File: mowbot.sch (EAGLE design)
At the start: 20 parts, among them Q1 PSMN9R1-30YL-MOSFET_N, Q2 PSMN9R1-30YL-MOSFET_N, Q3 PSMN9R1-30YL-MOSFET_N, Q4 PSMN9R1-30YL-MOSFET_N, Q5 PSMN9R1-30YL-MOSFET_N, Q6 PSMN9R1-30YL-MOSFET_N, Q7 PSMN9R1-30YL-MOSFET_N, Q8 PSMN9R1-30YL-MOSFET_N

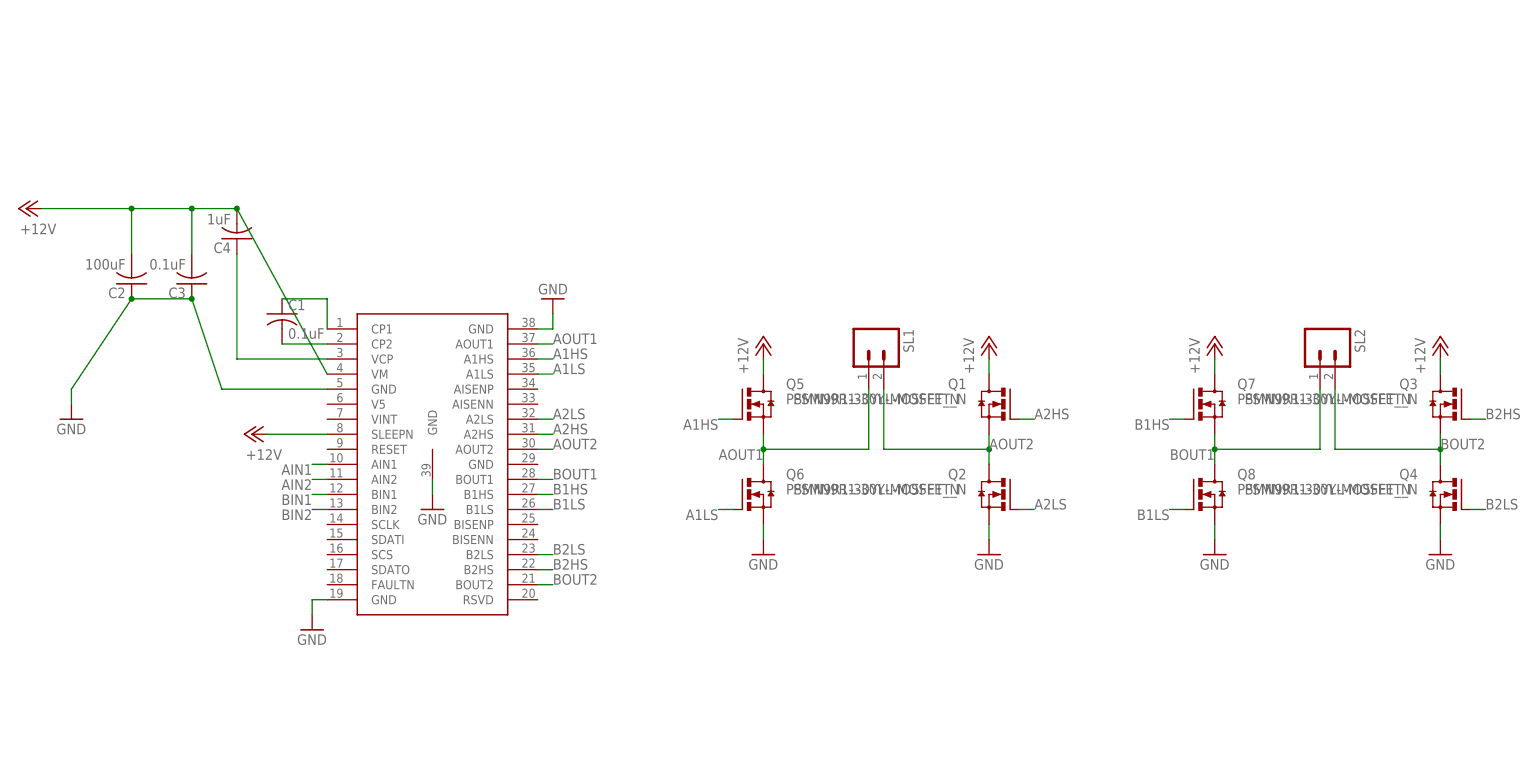
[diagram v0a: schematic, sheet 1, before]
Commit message: Arranged power FETs
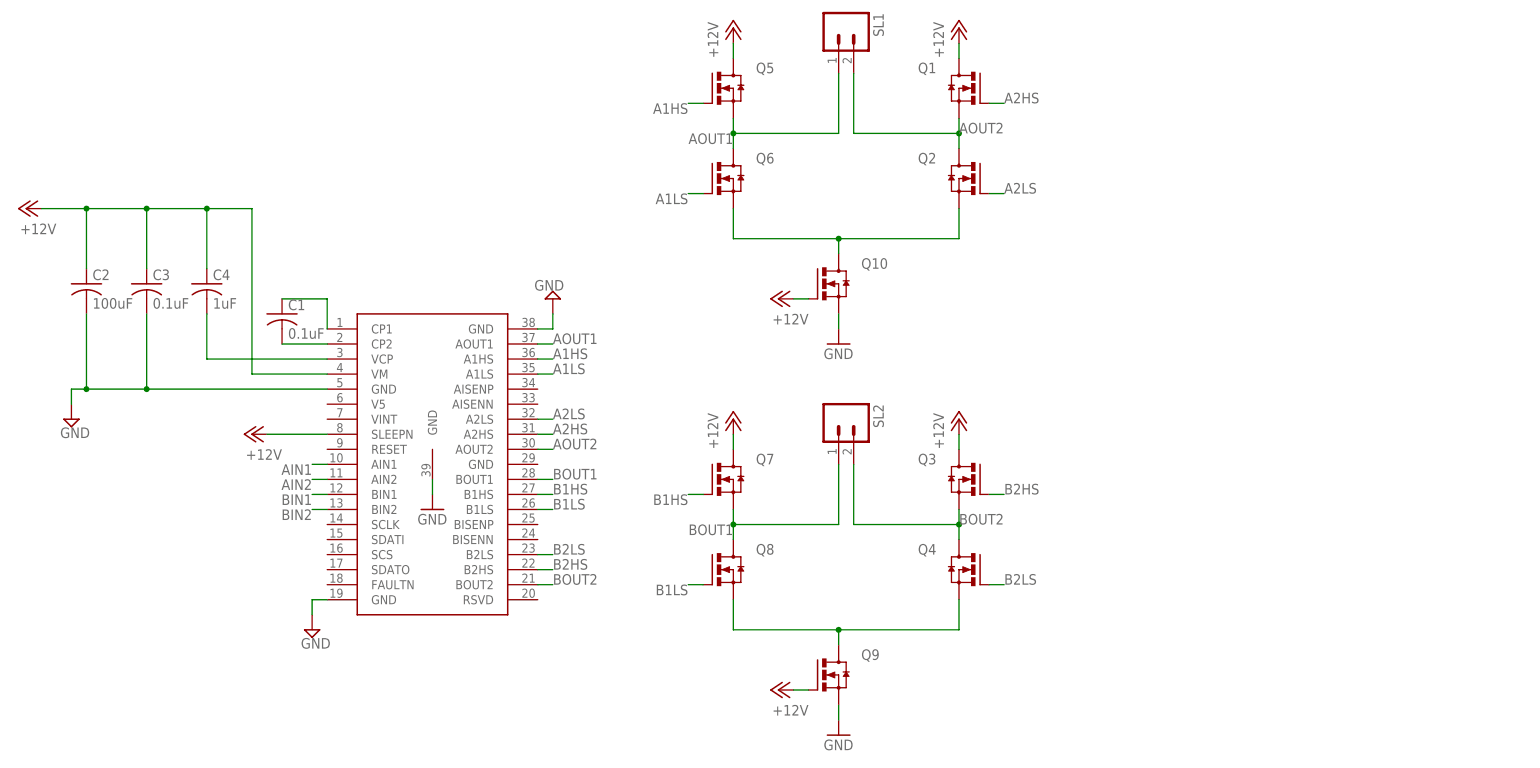
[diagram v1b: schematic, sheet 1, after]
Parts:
- added Q10, Q9: PSMN9R1-30YL-MOSFET_N, PSMN9R1-30YL_MOSFET_N:PSMN9R1-30YL-MOSFET_N
- added Q11: N-HEXFET_SOT323-, transistor-power:N-HEXFET_SOT323-
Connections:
- removed net N$7: C4.1, U$1.VCP
- new net N$2: C4.2, U$1.VCP
- new net N$4: Q4.S, Q8.S, Q9.D
- new net N$9: Q10.D, Q2.S, Q6.S
- net +12V: now also C2.1, C3.1, C4.1, Q10.G, Q11.G, Q9.G; no longer C2.2, C3.2, C4.2
- net GND: now also C2.2, C3.2, Q10.S, Q11.D, Q11.S, Q9.S; no longer C2.1, C3.1, Q2.S, Q4.S, Q6.S, Q8.S
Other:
- moved on the sheet: C2, C3, C4, Q1, Q2, Q3, Q4, Q5, Q6, Q7, Q8, SL1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

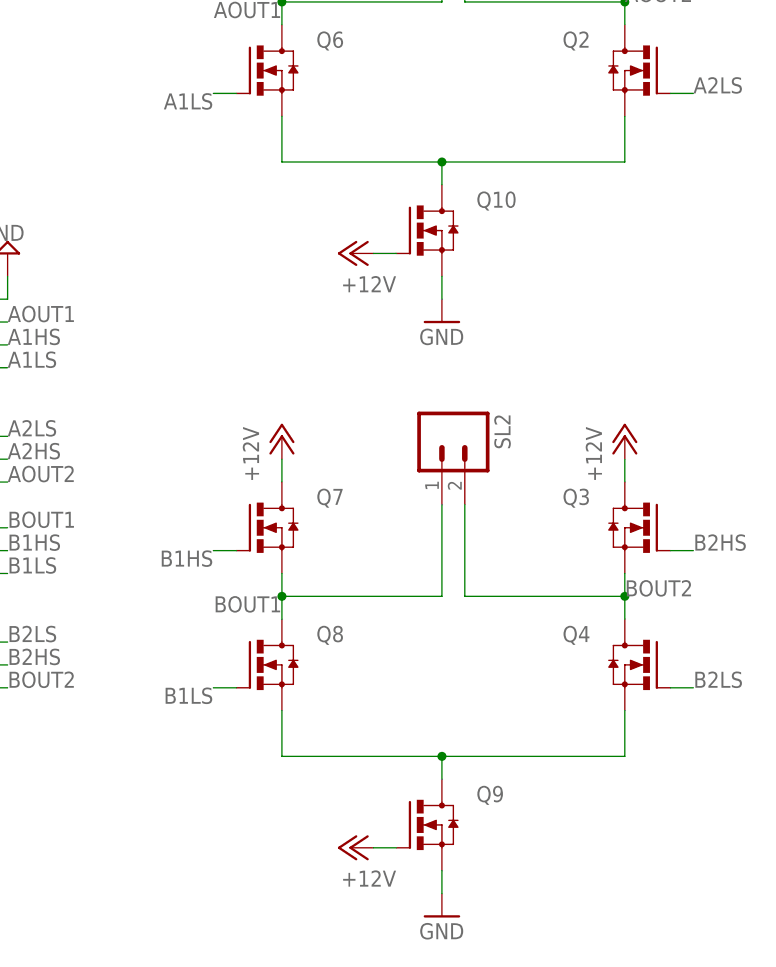
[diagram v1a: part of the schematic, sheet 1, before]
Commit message: Added reverse battery protection
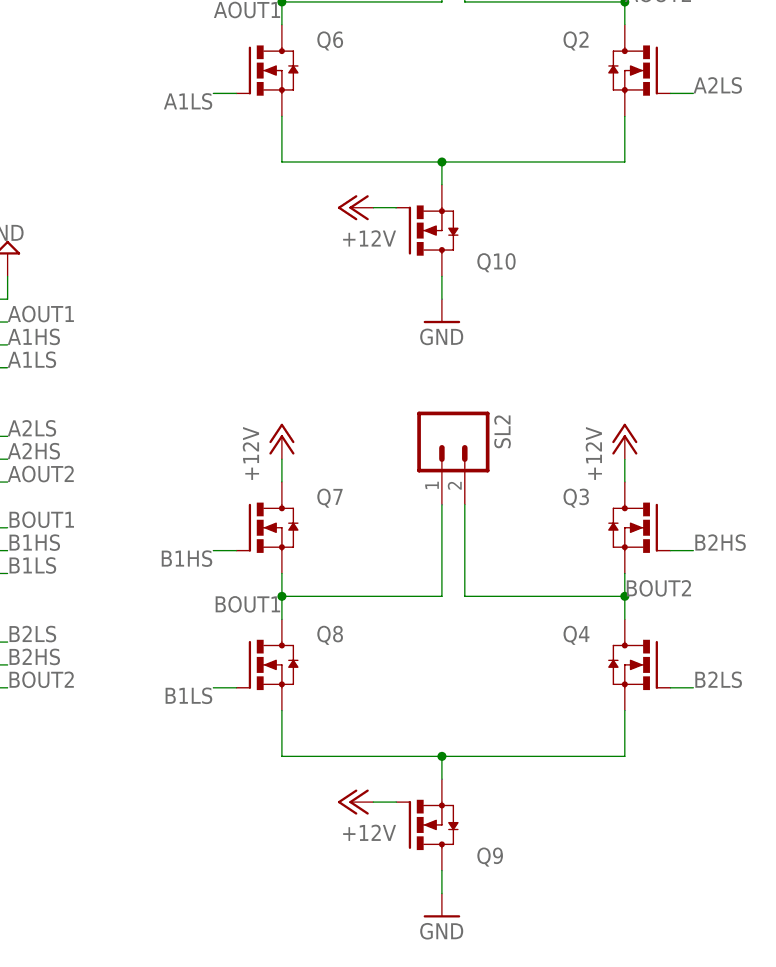
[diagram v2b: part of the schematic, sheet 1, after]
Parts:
- Q11: value N-HEXFET_SOT323- -> DMG2302UK-NMOSFET; device transistor-power:N-HEXFET_SOT323- -> DMG2302UK_NMOSFET:DMG2302UK-NMOSFET
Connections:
- net GND: now also Q10.D, Q9.D; no longer Q10.S, Q9.S
- net N$4: now also Q9.S; no longer Q9.D
- net N$9: now also Q10.S; no longer Q10.D
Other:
- moved on the sheet: Q10, Q9
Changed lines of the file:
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@@
 <part name="SUPPLY6" library="supply2" deviceset="GND" device=""/>
 <part name="SUPPLY7" library="supply2" deviceset="GND" device=""/>
-<part name="Q11" library="transistor-power" deviceset="N-HEXFET_?-*" device="SOT323"/>
+<part name="Q11" library="DMG2302UK_NMOSFET" deviceset="DMG2302UK-NMOSFET" device=""/>
 <part name="GND4" library="supply1" deviceset="GND" device=""/>
 <part name="P+10" library="supply1" deviceset="+12V" device=""/>
@@
 <instance part="C4" gate="G$1" x="-10.16" y="71.12"/>
 <instance part="P+6" gate="1" x="-2.54" y="45.72" rot="R90"/>
-<instance part="Q9" gate="G$1" x="93.98" y="5.08" smashed="yes">
-<attribute name="NAME" x="100.33" y="7.62" size="1.778" layer="95"/>
-</instance>
-<instance part="Q10" gate="G$1" x="93.98" y="71.12" smashed="yes">
-<attribute name="NAME" x="100.33" y="73.66" size="1.778" layer="95"/>
+<instance part="Q9" gate="G$1" x="93.98" y="5.08" smashed="yes" rot="MR180">
+<attribute name="NAME" x="100.33" y="2.54" size="1.778" layer="95" rot="MR180"/>
+</instance>
+<instance part="Q10" gate="G$1" x="93.98" y="71.12" smashed="yes" rot="MR180">
+<attribute name="NAME" x="100.33" y="68.58" size="1.778" layer="95" rot="MR180"/>
 </instance>
 <instance part="GND2" gate="1" x="96.52" y="-5.08"/>
-<instance part="P+8" gate="1" x="86.36" y="2.54" rot="R90"/>
+<instance part="P+8" gate="1" x="86.36" y="7.62" rot="R90"/>
 <instance part="GND3" gate="1" x="96.52" y="60.96"/>
-<instance part="P+9" gate="1" x="86.36" y="68.58" rot="R90"/>
+<instance part="P+9" gate="1" x="86.36" y="73.66" rot="R90"/>
 <instance part="SUPPLY5" gate="GND" x="-33.02" y="48.26"/>
 <instance part="SUPPLY6" gate="GND" x="7.62" y="12.7"/>
@@
 </segment>
 <segment>
+<pinref part="Q9" gate="G$1" pin="G"/>
 <pinref part="P+8" gate="1" pin="+12V"/>
-<pinref part="Q9" gate="G$1" pin="G"/>
-<wire x1="88.9" y1="2.54" x2="91.44" y2="2.54" width="0.1524" layer="91"/>
-</segment>
-<segment>
+<wire x1="91.44" y1="7.62" x2="88.9" y2="7.62" width="0.1524" layer="91"/>
+</segment>
+<segment>
+<pinref part="P+9" gate="1" pin="+12V"/>
 <pinref part="Q10" gate="G$1" pin="G"/>
-<pinref part="P+9" gate="1" pin="+12V"/>
-<wire x1="91.44" y1="68.58" x2="88.9" y2="68.58" width="0.1524" layer="91"/>
+<wire x1="88.9" y1="73.66" x2="91.44" y2="73.66" width="0.1524" layer="91"/>
 </segment>
 </net>
@@
 <pinref part="U$1" gate="G$1" pin="GND@5"/>
 <wire x1="27.94" y1="35.56" x2="27.94" y2="38.1" width="0.1524" layer="91"/>
-</segment>
-<segment>
-<pinref part="Q9" gate="G$1" pin="S"/>
-<pinref part="GND2" gate="1" pin="GND"/>
-<wire x1="96.52" y1="0" x2="96.52" y2="-2.54" width="0.1524" layer="91"/>
-</segment>
-<segment>
-<pinref part="Q10" gate="G$1" pin="S"/>
-<pinref part="GND3" gate="1" pin="GND"/>
-<wire x1="96.52" y1="66.04" x2="96.52" y2="63.5" width="0.1524" layer="91"/>
 </segment>
 <segment>
@@
 <pinref part="SUPPLY7" gate="GND" pin="GND"/>
 </segment>
+<segment>
+<pinref part="GND2" gate="1" pin="GND"/>
+<pinref part="Q9" gate="G$1" pin="D"/>
+<wire x1="96.52" y1="-2.54" x2="96.52" y2="0" width="0.1524" layer="91"/>
+</segment>
+<segment>
+<pinref part="Q10" gate="G$1" pin="D"/>
+<pinref part="GND3" gate="1" pin="GND"/>
+<wire x1="96.52" y1="66.04" x2="96.52" y2="63.5" width="0.1524" layer="91"/>
+</segment>
 </net>
 <net name="A1LS" class="0">
@@
 <pinref part="Q8" gate="G$1" pin="S"/>
 <wire x1="78.74" y1="12.7" x2="78.74" y2="17.78" width="0.1524" layer="91"/>
-<pinref part="Q9" gate="G$1" pin="D"/>
-<wire x1="96.52" y1="10.16" x2="96.52" y2="12.7" width="0.1524" layer="91"/>
-<wire x1="96.52" y1="12.7" x2="78.74" y2="12.7" width="0.1524" layer="91"/>
 <pinref part="Q4" gate="G$1" pin="S"/>
 <wire x1="116.84" y1="12.7" x2="116.84" y2="17.78" width="0.1524" layer="91"/>
+<wire x1="78.74" y1="12.7" x2="96.52" y2="12.7" width="0.1524" layer="91"/>
+<pinref part="Q9" gate="G$1" pin="S"/>
 <wire x1="96.52" y1="12.7" x2="116.84" y2="12.7" width="0.1524" layer="91"/>
+<wire x1="96.52" y1="10.16" x2="96.52" y2="12.7" width="0.1524" layer="91"/>
 <junction x="96.52" y="12.7"/>
 </segment>
@@
 <net name="N$9" class="0">
 <segment>
-<pinref part="Q10" gate="G$1" pin="D"/>
-<wire x1="96.52" y1="76.2" x2="96.52" y2="78.74" width="0.1524" layer="91"/>
 <pinref part="Q2" gate="G$1" pin="S"/>
+<wire x1="78.74" y1="78.74" x2="96.52" y2="78.74" width="0.1524" layer="91"/>
 <wire x1="96.52" y1="78.74" x2="116.84" y2="78.74" width="0.1524" layer="91"/>
 <wire x1="116.84" y1="78.74" x2="116.84" y2="83.82" width="0.1524" layer="91"/>
 <pinref part="Q6" gate="G$1" pin="S"/>
-<wire x1="96.52" y1="78.74" x2="78.74" y2="78.74" width="0.1524" layer="91"/>
 <wire x1="78.74" y1="78.74" x2="78.74" y2="83.82" width="0.1524" layer="91"/>
+<pinref part="Q10" gate="G$1" pin="S"/>
+<wire x1="96.52" y1="76.2" x2="96.52" y2="78.74" width="0.1524" layer="91"/>
 <junction x="96.52" y="78.74"/>
 </segment>
@@
 <instance part="SUPPLY3" gate="GND" x="93.98" y="91.44"/>
 <instance part="SUPPLY4" gate="GND" x="48.26" y="81.28" rot="R180"/>
-<instance part="Q11" gate="G$1" x="101.6" y="50.8"/>
-<instance part="GND4" gate="1" x="104.14" y="38.1"/>
-<instance part="P+10" gate="1" x="91.44" y="48.26" rot="R90"/>
+<instance part="Q11" gate="G$1" x="101.6" y="50.8" smashed="yes" rot="MR180">
+<attribute name="NAME" x="107.95" y="48.26" size="1.778" layer="95" rot="MR180"/>
+</instance>
+<instance part="GND4" gate="1" x="104.14" y="40.64"/>
+<instance part="P+10" gate="1" x="93.98" y="53.34" rot="R90"/>
 <instance part="SUPPLY8" gate="GND" x="104.14" y="60.96" rot="R180"/>
 </instances>
@@
 </segment>
 <segment>
+<pinref part="P+10" gate="1" pin="+12V"/>
 <pinref part="Q11" gate="G$1" pin="G"/>
-<pinref part="P+10" gate="1" pin="+12V"/>
-<wire x1="99.06" y1="48.26" x2="93.98" y2="48.26" width="0.1524" layer="91"/>
+<wire x1="96.52" y1="53.34" x2="99.06" y2="53.34" width="0.1524" layer="91"/>
 </segment>
 </net>
@@
 <segment>
 <pinref part="SUPPLY8" gate="GND" pin="GND"/>
+<pinref part="Q11" gate="G$1" pin="S"/>
+<wire x1="104.14" y1="58.42" x2="104.14" y2="55.88" width="0.1524" layer="91"/>
+</segment>
+<segment>
 <pinref part="Q11" gate="G$1" pin="D"/>
-<wire x1="104.14" y1="58.42" x2="104.14" y2="55.88" width="0.1524" layer="91"/>
-</segment>
-<segment>
-<pinref part="Q11" gate="G$1" pin="S"/>
 <pinref part="GND4" gate="1" pin="GND"/>
-<wire x1="104.14" y1="45.72" x2="104.14" y2="40.64" width="0.1524" layer="91"/>
-</segment>
-</net>
+<wire x1="104.14" y1="45.72" x2="104.14" y2="43.18" width="0.1524" layer="91"/>
+</segment>
+</net>

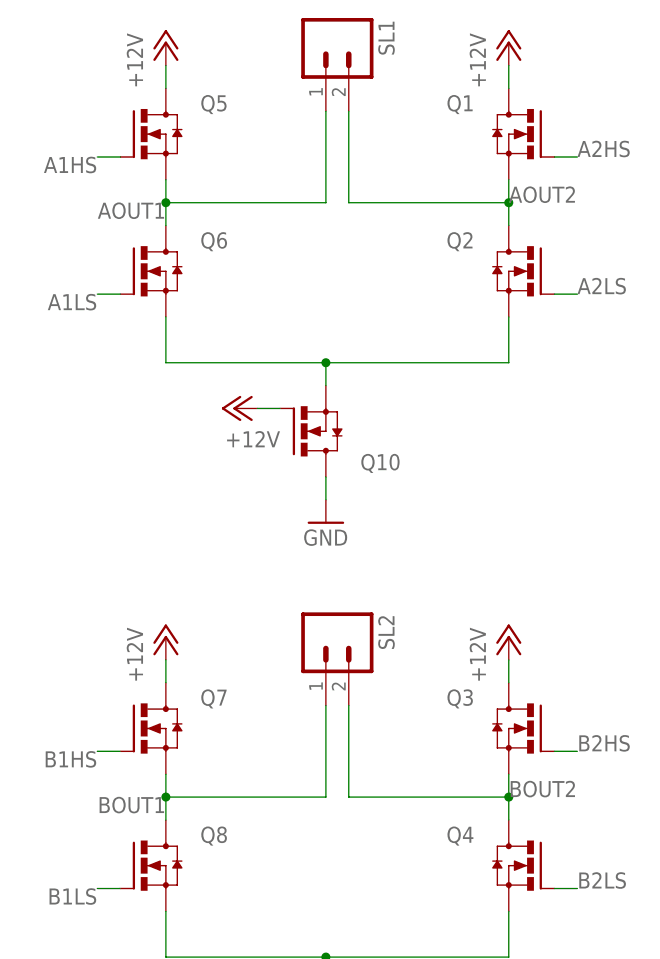
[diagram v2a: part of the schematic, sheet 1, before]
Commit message: replaced fets and routed them
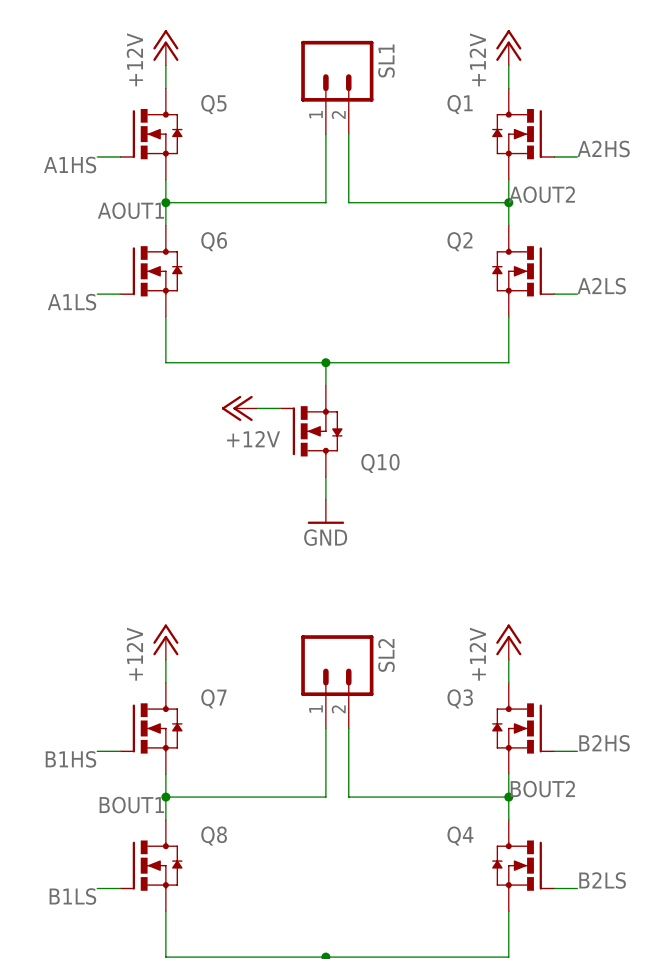
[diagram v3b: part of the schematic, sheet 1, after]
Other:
- moved on the sheet: SL1, SL2
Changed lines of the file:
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@@
 <attribute name="NAME" x="82.55" y="25.4" size="1.778" layer="95"/>
 </instance>
-<instance part="SL1" gate="G$1" x="96.52" y="114.3" rot="R270"/>
-<instance part="SL2" gate="G$1" x="96.52" y="48.26" rot="R270"/>
+<instance part="SL1" gate="G$1" x="96.52" y="111.76" rot="R270"/>
+<instance part="SL2" gate="G$1" x="96.52" y="45.72" rot="R270"/>
 <instance part="P+1" gate="1" x="78.74" y="114.3"/>
 <instance part="P+2" gate="1" x="116.84" y="114.3"/>
@@
 <pinref part="SL1" gate="G$1" pin="1"/>
 <wire x1="78.74" y1="96.52" x2="78.74" y2="93.98" width="0.1524" layer="91"/>
-<wire x1="96.52" y1="106.68" x2="96.52" y2="96.52" width="0.1524" layer="91"/>
+<wire x1="96.52" y1="104.14" x2="96.52" y2="96.52" width="0.1524" layer="91"/>
 <wire x1="78.74" y1="96.52" x2="96.52" y2="96.52" width="0.1524" layer="91"/>
 <junction x="78.74" y="96.52"/>
@@
 <pinref part="SL2" gate="G$1" pin="1"/>
 <wire x1="78.74" y1="30.48" x2="78.74" y2="27.94" width="0.1524" layer="91"/>
-<wire x1="96.52" y1="40.64" x2="96.52" y2="30.48" width="0.1524" layer="91"/>
+<wire x1="96.52" y1="38.1" x2="96.52" y2="30.48" width="0.1524" layer="91"/>
 <wire x1="96.52" y1="30.48" x2="78.74" y2="30.48" width="0.1524" layer="91"/>
 <junction x="78.74" y="30.48"/>
@@
 <wire x1="116.84" y1="30.48" x2="116.84" y2="27.94" width="0.1524" layer="91"/>
 <wire x1="116.84" y1="30.48" x2="99.06" y2="30.48" width="0.1524" layer="91"/>
-<wire x1="99.06" y1="30.48" x2="99.06" y2="40.64" width="0.1524" layer="91"/>
+<wire x1="99.06" y1="30.48" x2="99.06" y2="38.1" width="0.1524" layer="91"/>
 <junction x="116.84" y="30.48"/>
 <label x="116.84" y="30.48" size="1.778" layer="95"/>
@@
 <segment>
 <pinref part="Q1" gate="G$1" pin="S"/>
-<pinref part="Q2" gate="G$1" pin="D"/>
 <wire x1="116.84" y1="99.06" x2="116.84" y2="96.52" width="0.1524" layer="91"/>
 <pinref part="SL1" gate="G$1" pin="2"/>
-<wire x1="116.84" y1="96.52" x2="116.84" y2="93.98" width="0.1524" layer="91"/>
-<wire x1="99.06" y1="106.68" x2="99.06" y2="96.52" width="0.1524" layer="91"/>
+<wire x1="99.06" y1="104.14" x2="99.06" y2="96.52" width="0.1524" layer="91"/>
 <wire x1="99.06" y1="96.52" x2="116.84" y2="96.52" width="0.1524" layer="91"/>
+<label x="116.84" y="96.52" size="1.778" layer="95"/>
+<pinref part="Q2" gate="G$1" pin="D"/>
+<wire x1="116.84" y1="93.98" x2="116.84" y2="96.52" width="0.1524" layer="91"/>
 <junction x="116.84" y="96.52"/>
-<label x="116.84" y="96.52" size="1.778" layer="95"/>
 </segment>
 </net>
@@
 <net name="N$9" class="0">
 <segment>
-<pinref part="Q2" gate="G$1" pin="S"/>
 <wire x1="78.74" y1="78.74" x2="96.52" y2="78.74" width="0.1524" layer="91"/>
 <wire x1="96.52" y1="78.74" x2="116.84" y2="78.74" width="0.1524" layer="91"/>
-<wire x1="116.84" y1="78.74" x2="116.84" y2="83.82" width="0.1524" layer="91"/>
 <pinref part="Q6" gate="G$1" pin="S"/>
 <wire x1="78.74" y1="78.74" x2="78.74" y2="83.82" width="0.1524" layer="91"/>
@@
 <wire x1="96.52" y1="76.2" x2="96.52" y2="78.74" width="0.1524" layer="91"/>
 <junction x="96.52" y="78.74"/>
-</segment>
-</net>
+<pinref part="Q2" gate="G$1" pin="S"/>
+<wire x1="116.84" y1="78.74" x2="116.84" y2="83.82" width="0.1524" layer="91"/>
+</segment>
+</net>
